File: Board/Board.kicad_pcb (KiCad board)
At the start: 2 copper layers, 35 parts, among them J1 Micro_SD_Card, J2 Conn_01x02_Male, Q1 Q_NMOS_GSD, Q2 Q_NMOS_GSD, SW2 SW_SPST, U1 ATmega328P-AU, U2 TPS613221ADBV, Y1 10MHz

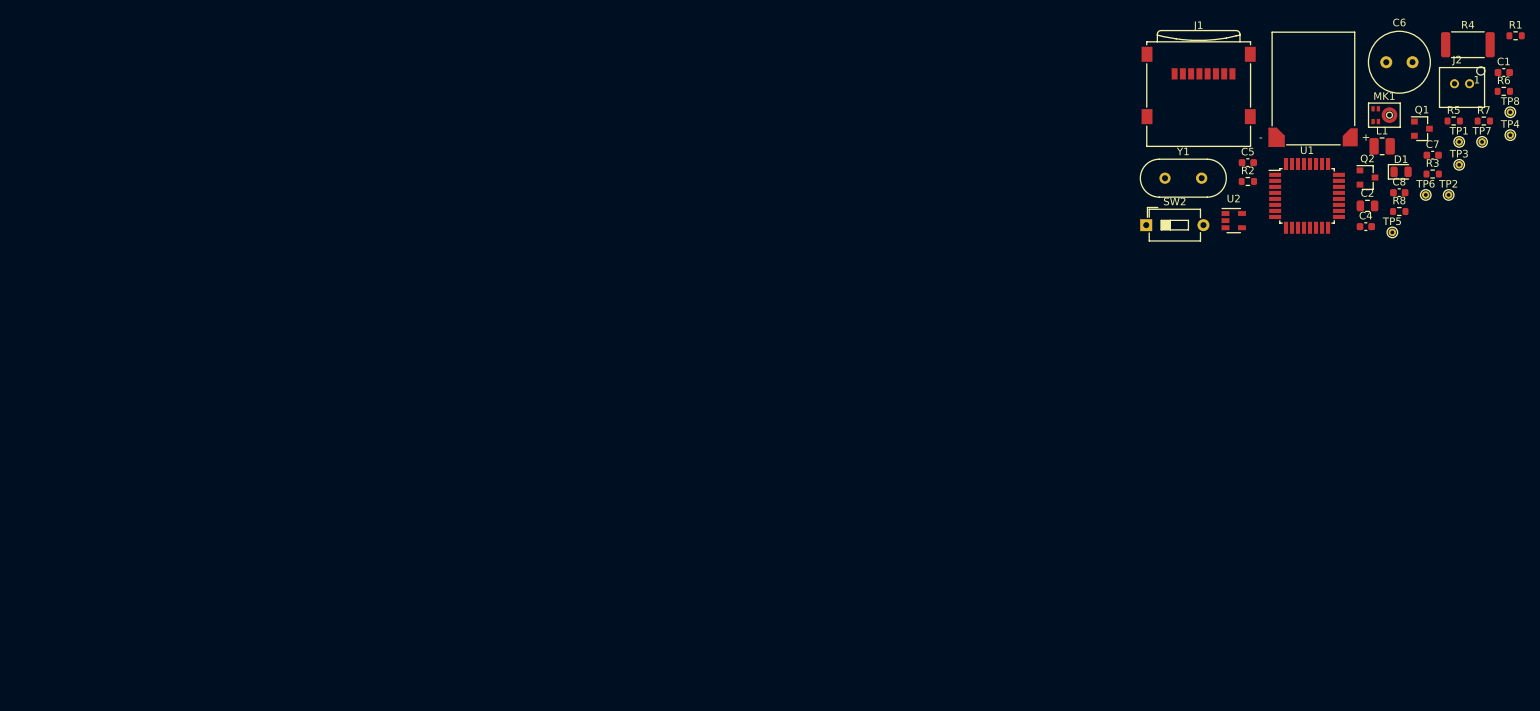
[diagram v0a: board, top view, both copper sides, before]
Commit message: Changed components + first layout tests
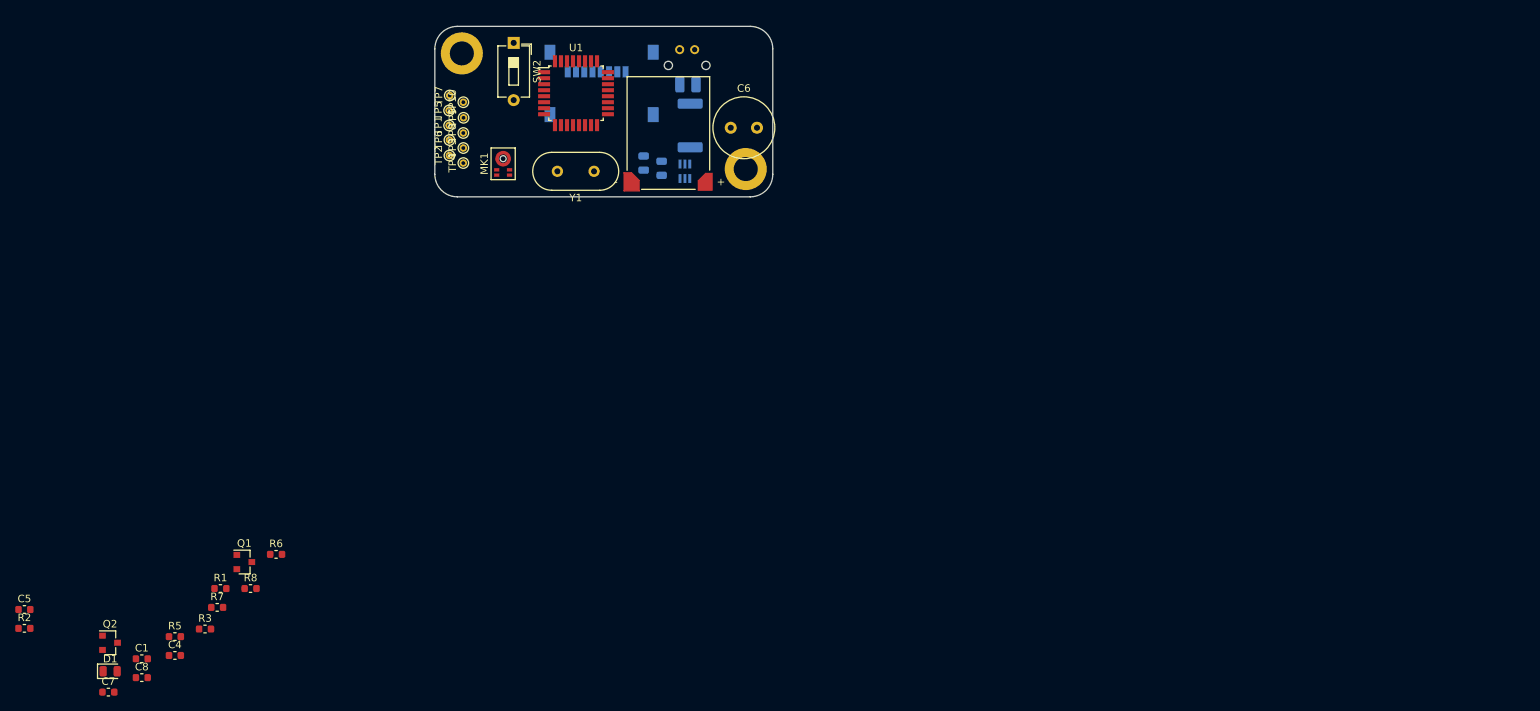
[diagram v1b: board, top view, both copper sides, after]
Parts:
- added C3: 10uF, Capacitor_SMD:C_0805_2012Metric, B.Cu at (50.2, 38.9)
- added REF**: MountingHole_3.2mm_M3_DIN965_Pad, MountingHole:MountingHole_3.2mm_M3_DIN965_Pad, F.Cu at (61.4, 39.0)
- added REF**: MountingHole_3.2mm_M3_DIN965_Pad, MountingHole:MountingHole_3.2mm_M3_DIN965_Pad, F.Cu at (23.6, 23.6)
- added TP10: TestPoint, TestPoint:TestPoint_THTPad_D1.0mm_Drill0.5mm, F.Cu at (23.8, 30.1)
- added TP9: TestPoint, TestPoint:TestPoint_THTPad_D1.0mm_Drill0.5mm, F.Cu at (23.8, 32.2)
- C2: value 22uF -> 10uF; moved to B.Cu
- J1, L1, R4: moved to B.Cu
- J2: footprint ConnectorsEvo:B02B-PASK -> ConnectorsEvo:S02B-PASK; moved to B.Cu
- U2: value TPS613221ADBV -> TLV61225DCKR; footprint Package_TO_SOT_SMD:SOT-23-5 -> Board:SOT65P210X110-6N; moved to B.Cu
- moved C1 197.4 mm to (-19.0, 104.2)
- moved C7 190.3 mm to (-23.5, 108.6)
- moved R1 187.5 mm to (-8.54, 94.9)
- moved D1 184.3 mm to (-23.2, 105.9)
- moved R5 183.6 mm to (-14.6, 101.3)
- moved R7 180.7 mm to (-8.97, 97.4)
- moved C8 179.4 mm to (-19.0, 106.7)
- moved Q2 178.5 mm to (-23.2, 102.1)
- moved R6 174.7 mm to (-1.13, 90.3)
- moved R3 174.3 mm to (-10.6, 100.2)
- moved C5 173.4 mm to (-34.6, 97.6)
- moved R2 173.4 mm to (-34.6, 100.2)
- moved C4 168.5 mm to (-14.6, 103.8)
- moved Q1 167.1 mm to (-5.36, 91.3)
- moved R8 161.0 mm to (-4.53, 94.9)
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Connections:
- C2 pad 1: +3V3 -> +BATT
- U2 pad 1: Net-(L1-Pad2) -> +BATT
- U2 pad 2: GND -> +3V3
- U2 pad 3: Net-(U2-Pad3) -> GND
- U2 pad 5: Net-(U2-Pad5) -> Net-(L1-Pad2)
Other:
- board outline added: 45 x 22.7 mm

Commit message: First PCB
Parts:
- added C9: 100nF, Capacitor_SMD:C_0603_1608Metric, F.Cu at (34.5, 38.7)
- C1, D1, MK1, R1, R2: moved to B.Cu
- moved C7 104.2 mm to (43.2, 28.6)
- moved C8 101.0 mm to (43.2, 27.1)
- moved D1 100.4 mm to (35.4, 24.4)
- moved R2 100.3 mm to (31.1, 24.4), turned to 180 degrees
- moved C1 99.1 mm to (41.0, 25.3)
- moved C5 90.3 mm to (27.7, 32.3), turned to 90 degrees
- moved Q2 88.9 mm to (39.0, 38.6), turned to 270 degrees
- moved R5 87.6 mm to (42.9, 35.2), turned to 180 degrees
- moved C4 85.7 mm to (27.7, 29.2), turned to 90 degrees
- moved R3 82.5 mm to (42.9, 37.5), turned to 180 degrees
- moved R1 79.7 mm to (28.2, 24.1), turned to 270 degrees
- moved R8 77.5 mm to (42.9, 33.6), turned to 180 degrees
- moved Q1 70.5 mm to (43.1, 40.1)
- moved R7 70.4 mm to (28.9, 38.0)
- moved R6 68.3 mm to (39.4, 35.3), turned to 90 degrees
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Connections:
- net SDGND renamed Net-(J1-Pad6)
- REF** pad 1: (no net) -> GND (x2)
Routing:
- net +3V3: track 0.00 -> 58.7 mm, vias 0 -> 4
- net MCU_POWER: track 0.00 -> 50.9 mm, vias 0 -> 3
- net +BATT: track 0.00 -> 37.6 mm, vias 0 -> 1
- net /RESET: track 0.00 -> 23.7 mm, vias 0 -> 1
- net /MICCLK: track 0.00 -> 15.9 mm, vias 0 -> 2
- net /SCK: track 0.00 -> 15.7 mm, vias 0 -> 2
- net /SD_POWER: track 0.00 -> 14.2 mm, vias 0 -> 2
- net Net-(R7-Pad1): track 0.00 -> 13.1 mm
- net /MOSI: track 0.00 -> 12.9 mm, vias 0 -> 1
- net GND: track 0.00 -> 12.1 mm, vias 0 -> 4
- net Net-(D1-Pad2): track 0.00 -> 11.9 mm, vias 0 -> 1
- net /SPEAKER: track 0.00 -> 11.5 mm, vias 0 -> 2
- net /MISO: track 0.00 -> 10.2 mm, vias 0 -> 1
- net /MICDATA: track 0.00 -> 8.72 mm
- net /CS: track 0.00 -> 8.12 mm, vias 0 -> 1
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- added copper zone on B.Cu, net GND
- added copper zone on F.Cu, net GND
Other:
- outline, holes or cut-outs redrawn

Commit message: PCB almost done
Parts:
- moved TP4 1.00 mm to (33.6, 41.2)
- moved TP5 1.00 mm to (35.8, 41.2)
- moved TP6 1.00 mm to (31.4, 41.2)
- moved TP7 1.00 mm to (29.2, 41.2)
- moved TP1 0.10 mm to (23.1, 41.2)
- moved TP2 0.10 mm to (25.3, 41.2)
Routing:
- net MCU_POWER: track 50.9 -> 52.0 mm, vias 3 -> 4
- net +BATT: track 37.6 -> 38.6 mm, vias 1 -> 3
- net /SCK: track 15.7 -> 15.2 mm
- net /MOSI: track 12.9 -> 12.4 mm
- net /MISO: track 10.2 -> 9.69 mm
- net Net-(R7-Pad1): track 13.1 -> 12.7 mm, vias 0 -> 1
- net GND: vias 4 -> 12
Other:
- board text added: "5V"
- board text added: "GND"
- board text added: "GND/BATT"
- board text added: "MISO"
- board text added: "MOSI"
- board text added: "PROG"
- board text added: "RST"
- board text added: "RUN"
- board text added: "RX"
- board text added: "SCK"
- board text added: "SW+"
- board text added: "SW-"
- board text added: "TX"

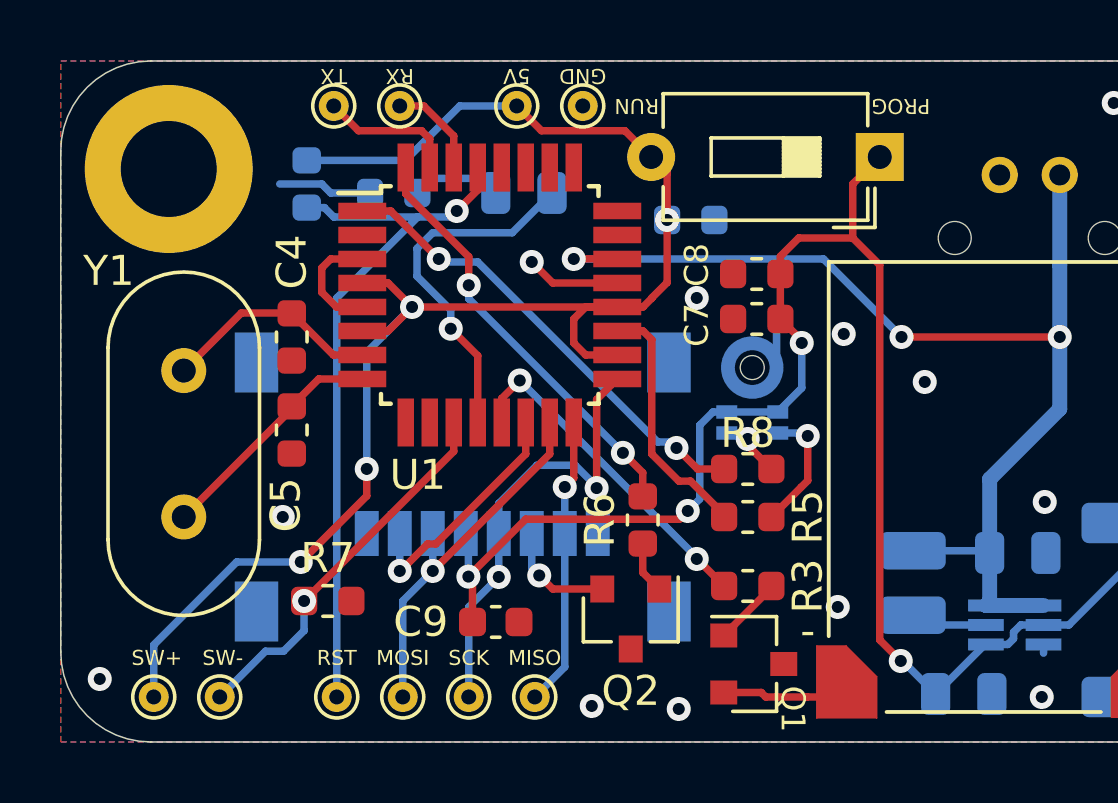
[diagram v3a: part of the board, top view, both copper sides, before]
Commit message: Replaced SD connector by correct one
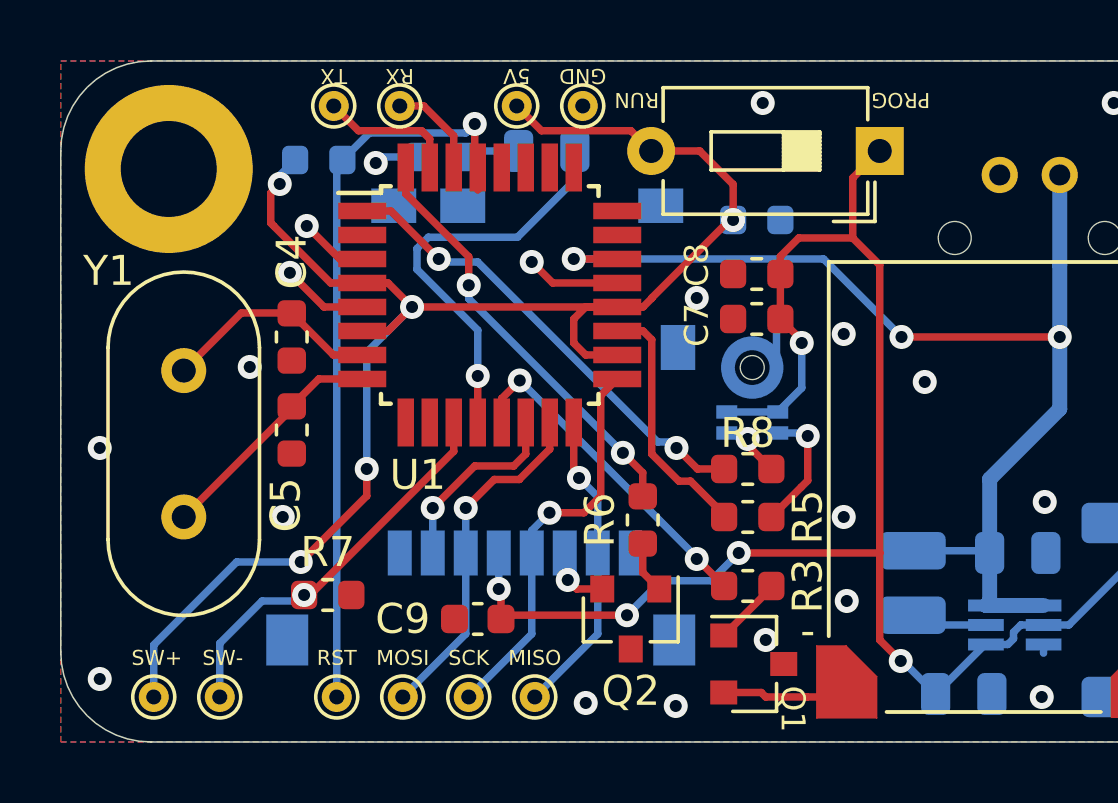
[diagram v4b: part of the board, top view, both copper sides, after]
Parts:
- J1: value Micro_SD_Card -> 5025700893; footprint Connector_Card:microSD_HC_Wuerth_693072010801 -> Board:MOLEX_5025700893
- moved C1 2.20 mm to (43.2, 25.3)
- moved J1 2.09 mm to (34.0, 32.2)
- moved R2 2.00 mm to (32.7, 23.2)
- moved D1 1.59 mm to (36.2, 23.0)
- moved R1 0.89 mm to (28.6, 23.3), turned to 0 degrees
- moved C9 0.61 mm to (33.9, 38.6), turned to 180 degrees
- moved R7 0.20 mm to (28.9, 37.8)
- moved SW2 0.20 mm to (47.3, 23.0)
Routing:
- net Net-(D1-Pad2): track 11.9 -> 13.8 mm
- net /SCK: track 15.2 -> 13.3 mm, vias 2 -> 1
- net /CS: track 8.12 -> 6.40 mm
- net Net-(J1-Pad6): track 3.79 -> 2.22 mm
- net MCU_POWER: track 52.0 -> 53.6 mm, vias 4 -> 5
- net Net-(D1-Pad1): track 3.01 -> 1.86 mm
- net /MISO: track 9.69 -> 10.7 mm
- net /RESET: track 24.1 -> 25.1 mm
- net /MOSI: track 12.4 -> 11.7 mm
- net +3V3: track 58.7 -> 59.3 mm, vias 4 -> 5
- net GND: track 12.1 -> 11.8 mm, vias 12 -> 20
